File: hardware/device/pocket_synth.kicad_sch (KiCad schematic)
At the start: 7 parts

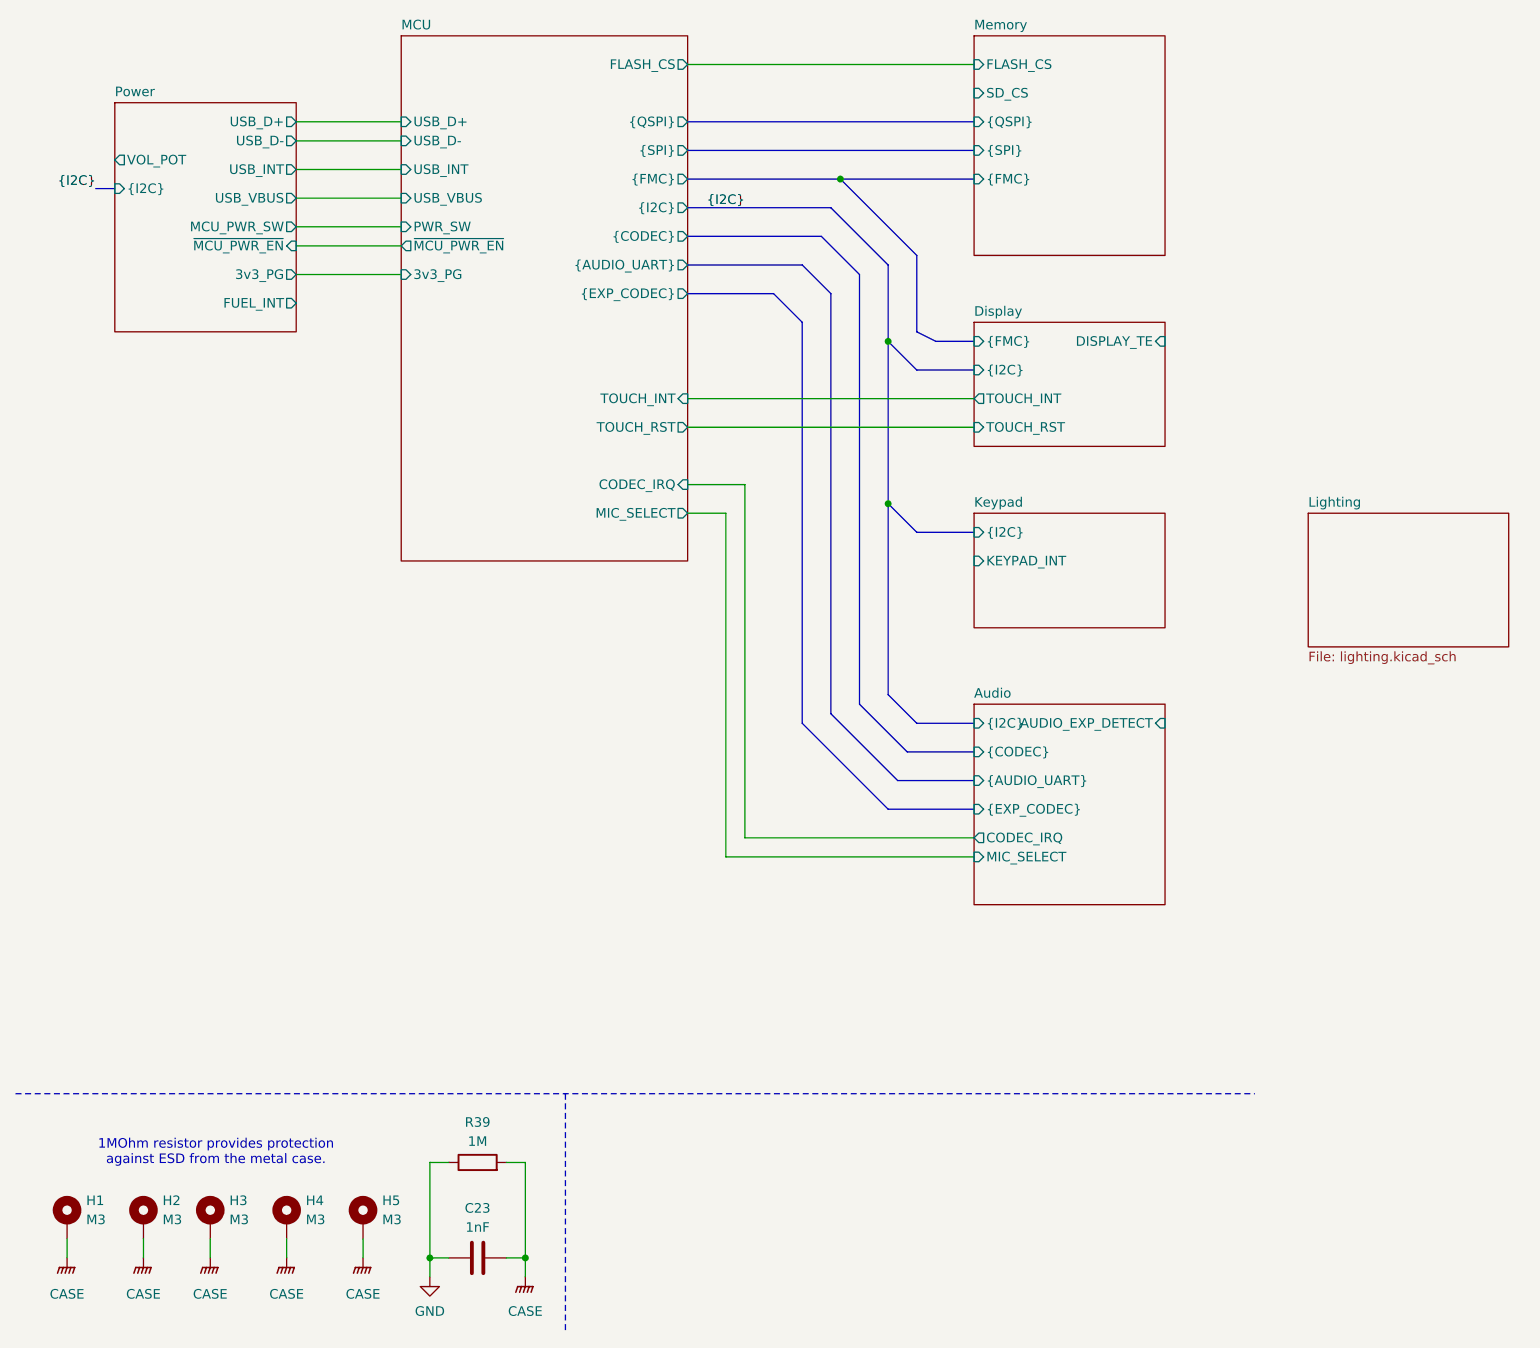
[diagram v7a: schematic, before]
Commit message: feat: start replacing expansion  port with bluetooth module
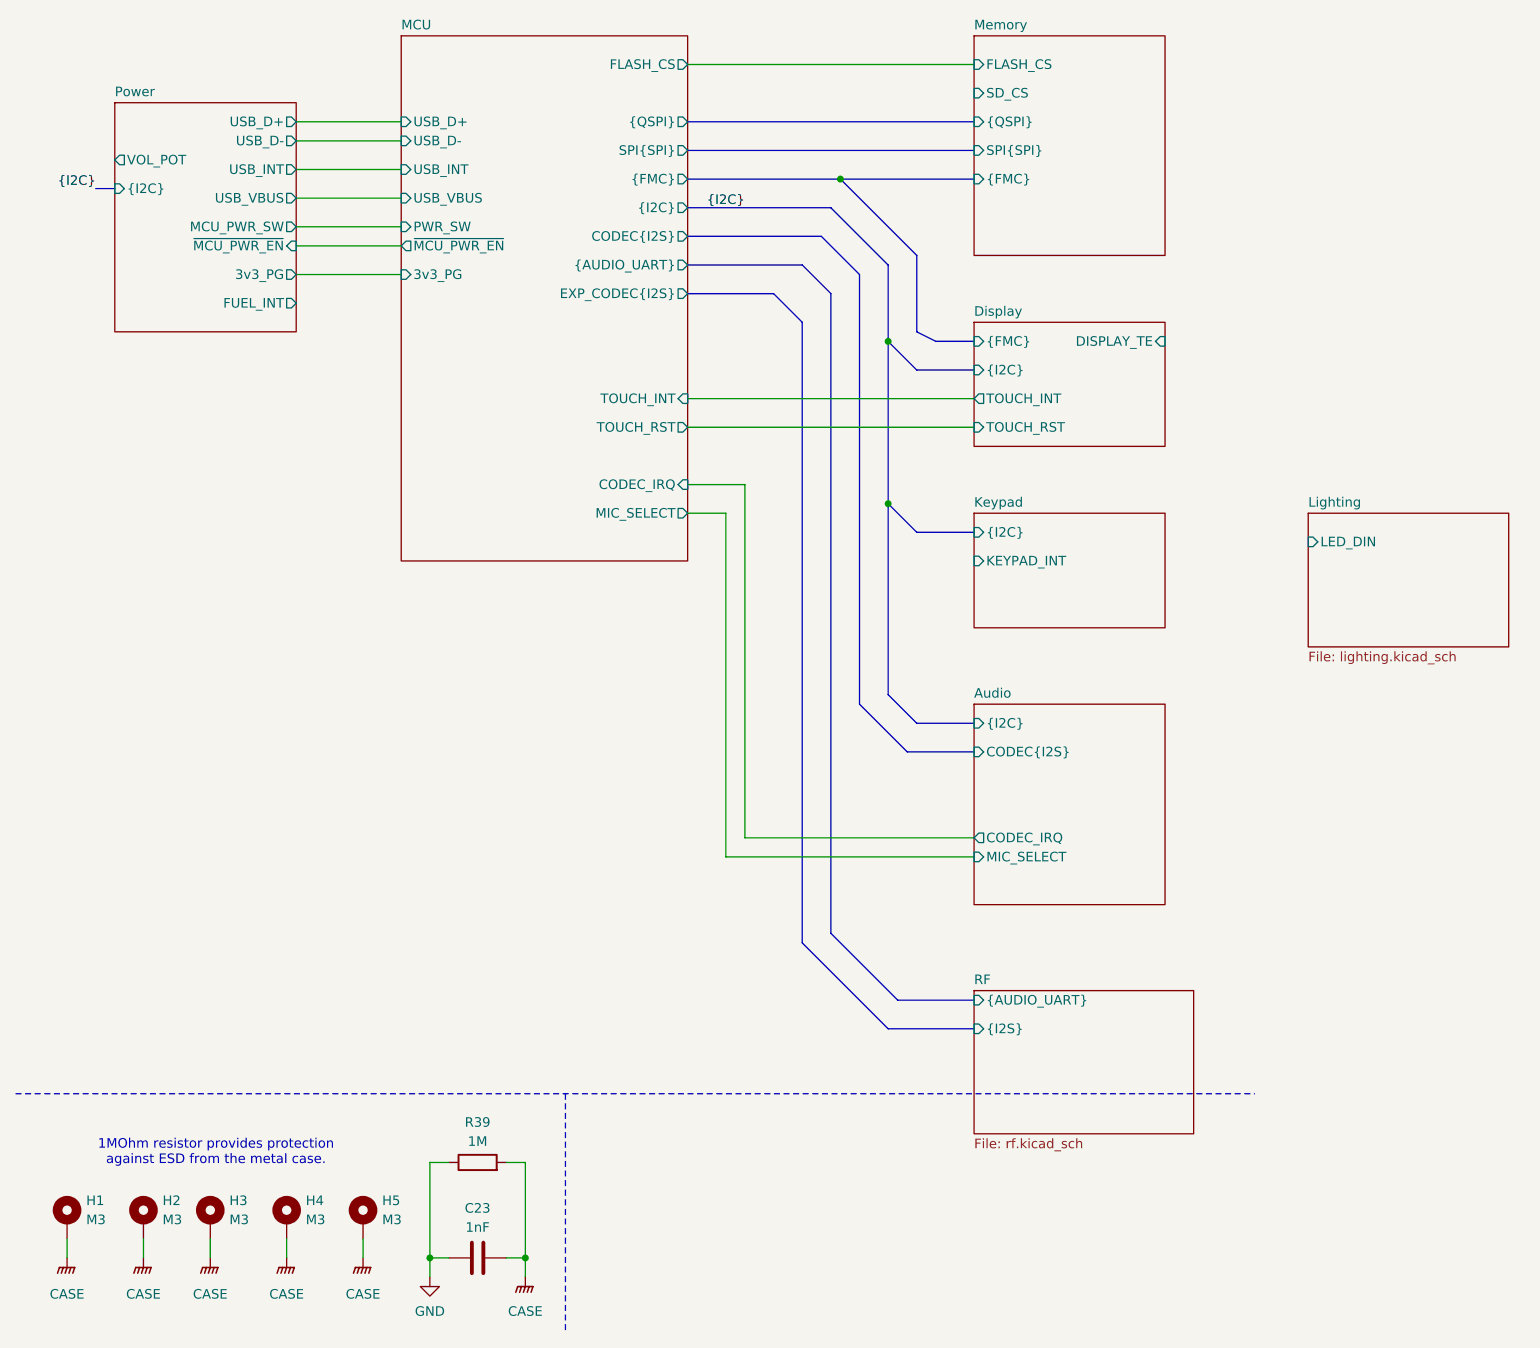
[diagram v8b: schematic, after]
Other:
- added sheet RF (rf.kicad_sch)
- sheet Audio ports: added CODEC{I2S}; removed AUDIO_EXP_DETECT, {AUDIO_UART}, {CODEC}, {EXP_CODEC}
- sheet Lighting ports: added LED_DIN; removed none
- sheet MCU ports: added CODEC{I2S}, EXP_CODEC{I2S}, SPI{SPI}; removed {CODEC}, {EXP_CODEC}, {SPI}
- sheet Memory ports: added SPI{SPI}; removed {SPI}
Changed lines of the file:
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@@
 		)
+	)
+	(bus_alias "I2S"
+		(members "MCLK" "ADCDAT" "DACDAT" "LRCLK" "BCLK")
 	)
 	(text "1MOhm resistor provides protection\nagainst ESD from the metal case."
@@
 		(color 0 0 0 0)
 	)
+	(bus
+		(pts
+			(xy 128.27 157.48) (xy 139.7 157.48)
+		)
+		(stroke
+			(width 0)
+			(type default)
+		)
+	)
 	(wire
 		(pts
@@
 	(bus
 		(pts
+			(xy 116.84 146.05) (xy 128.27 157.48)
+		)
+		(stroke
+			(width 0)
+			(type default)
+		)
+	)
+	(bus
+		(pts
 			(xy 132.08 116.84) (xy 139.7 116.84)
 		)
@@
 	(bus
 		(pts
+			(xy 120.65 144.78) (xy 129.54 153.67)
+		)
+		(stroke
+			(width 0)
+			(type default)
+		)
+	)
+	(bus
+		(pts
 			(xy 101.6 52.07) (xy 119.38 52.07)
 		)
@@
 	(bus
 		(pts
-			(xy 116.84 63.5) (xy 116.84 116.84)
-		)
-		(stroke
-			(width 0)
-			(type default)
-		)
-	)
-	(bus
-		(pts
 			(xy 101.6 40.64) (xy 139.7 40.64)
+		)
+		(stroke
+			(width 0)
+			(type default)
+		)
+	)
+	(bus
+		(pts
+			(xy 130.81 120.65) (xy 139.7 120.65)
+		)
+		(stroke
+			(width 0)
+			(type default)
+		)
+	)
+	(bus
+		(pts
+			(xy 116.84 63.5) (xy 116.84 146.05)
+		)
+		(stroke
+			(width 0)
+			(type default)
+		)
+	)
+	(bus
+		(pts
+			(xy 120.65 59.69) (xy 120.65 144.78)
 		)
 		(stroke
@@
 		)
 	)
-	(bus
-		(pts
-			(xy 120.65 59.69) (xy 120.65 115.57)
-		)
-		(stroke
-			(width 0)
-			(type default)
-		)
-	)
 	(wire
 		(pts
@@
 	(bus
 		(pts
-			(xy 130.81 120.65) (xy 139.7 120.65)
-		)
-		(stroke
-			(width 0)
-			(type default)
-		)
-	)
-	(bus
-		(pts
 			(xy 124.46 114.3) (xy 130.81 120.65)
 		)
@@
 		)
 	)
-	(bus
-		(pts
-			(xy 129.54 124.46) (xy 139.7 124.46)
-		)
-		(stroke
-			(width 0)
-			(type default)
-		)
-	)
 	(wire
 		(pts
@@
 		)
 	)
-	(bus
-		(pts
-			(xy 128.27 128.27) (xy 139.7 128.27)
-		)
-		(stroke
-			(width 0)
-			(type default)
-		)
-	)
 	(wire
 		(pts
@@
 	(bus
 		(pts
-			(xy 120.65 115.57) (xy 129.54 124.46)
-		)
-		(stroke
-			(width 0)
-			(type default)
-		)
-	)
-	(bus
-		(pts
 			(xy 101.6 44.45) (xy 121.92 44.45)
 		)
@@
 	(bus
 		(pts
-			(xy 116.84 116.84) (xy 128.27 128.27)
-		)
-		(stroke
-			(width 0)
-			(type default)
-		)
-	)
-	(bus
-		(pts
 			(xy 119.38 52.07) (xy 124.46 57.15)
+		)
+		(stroke
+			(width 0)
+			(type default)
+		)
+	)
+	(bus
+		(pts
+			(xy 129.54 153.67) (xy 139.7 153.67)
 		)
 		(stroke
@@
 			)
 		)
-		(pin "{SPI}" output
-			(at 101.6 40.64 0)
-			(effects
-				(font
-					(size 1.27 1.27)
-				)
-				(justify right)
-			)
-		)
 		(pin "USB_D+" input
 			(at 63.5 36.83 180)
@@
 			)
 		)
-		(pin "{CODEC}" output
-			(at 101.6 52.07 0)
-			(effects
-				(font
-					(size 1.27 1.27)
-				)
-				(justify right)
-			)
-		)
 		(pin "~{MCU_PWR_EN}" output
 			(at 63.5 53.34 180)
@@
 			)
 		)
-		(pin "{EXP_CODEC}" output
-			(at 101.6 59.69 0)
-			(effects
-				(font
-					(size 1.27 1.27)
-				)
-				(justify right)
-			)
-		)
 		(pin "{QSPI}" output
 			(at 101.6 36.83 0)
@@
 				)
 				(justify left)
+			)
+		)
+		(pin "CODEC{I2S}" output
+			(at 101.6 52.07 0)
+			(effects
+				(font
+					(size 1.27 1.27)
+				)
+				(justify right)
+			)
+		)
+		(pin "EXP_CODEC{I2S}" output
+			(at 101.6 59.69 0)
+			(effects
+				(font
+					(size 1.27 1.27)
+				)
+				(justify right)
+			)
+		)
+		(pin "SPI{SPI}" output
+			(at 101.6 40.64 0)
+			(effects
+				(font
+					(size 1.27 1.27)
+				)
+				(justify right)
 			)
 		)
@@
 	)
 	(sheet
+		(at 139.7 152.4)
+		(size 29.21 19.05)
+		(exclude_from_sim no)
+		(in_bom yes)
+		(on_board yes)
+		(dnp no)
+		(fields_autoplaced yes)
+		(stroke
+			(width 0.1524)
+			(type solid)
+		)
+		(fill
+			(color 0 0 0 0.0000)
+		)
+		(property "Sheetname" "RF"
+			(at 139.7 151.6884 0)
+			(effects
+				(font
+					(size 1.27 1.27)
+				)
+				(justify left bottom)
+			)
+		)
+		(property "Sheetfile" "rf.kicad_sch"
+			(at 139.7 172.0346 0)
+			(effects
+				(font
+					(size 1.27 1.27)
+				)
+				(justify left top)
+			)
+		)
+		(pin "{I2S}" input
+			(at 139.7 157.48 180)
+			(effects
+				(font
+					(size 1.27 1.27)
+				)
+				(justify left)
+			)
+		)
+		(pin "{AUDIO_UART}" input
+			(at 139.7 153.67 180)
+			(effects
+				(font
+					(size 1.27 1.27)
+				)
+				(justify left)
+			)
+		)
+		(instances
+			(project "pocket_synth"
+				(path "/485383b8-00f4-4405-b270-de249939cff4"
+					(page "9")
+				)
+			)
+		)
+	)
+	(sheet
 		(at 139.7 88.9)
 		(size 25.4 15.24)
@@
 			)
 		)
-		(pin "{CODEC}" input
-			(at 139.7 120.65 180)
-			(effects
-				(font
-					(size 1.27 1.27)
-				)
-				(justify left)
-			)
-		)
 		(pin "{I2C}" input
 			(at 139.7 116.84 180)
@@
 			)
 		)
-		(pin "AUDIO_EXP_DETECT" input
-			(at 165.1 116.84 0)
-			(effects
-				(font
-					(size 1.27 1.27)
-				)
-				(justify right)
-			)
-		)
-		(pin "{AUDIO_UART}" input
-			(at 139.7 124.46 180)
-			(effects
-				(font
-					(size 1.27 1.27)
-				)
-				(justify left)
-			)
-		)
 		(pin "MIC_SELECT" input
 			(at 139.7 134.62 180)
@@
 			)
 		)
-		(pin "{EXP_CODEC}" input
-			(at 139.7 128.27 180)
+		(pin "CODEC{I2S}" input
+			(at 139.7 120.65 180)
 			(effects
 				(font
@@
 			)
 		)
-		(pin "{SPI}" input
-			(at 139.7 40.64 180)
-			(effects
-				(font
-					(size 1.27 1.27)
-				)
-				(justify left)
-			)
-		)
 		(pin "{QSPI}" input
 			(at 139.7 36.83 180)
@@
 		(pin "FLASH_CS" input
 			(at 139.7 29.21 180)
+			(effects
+				(font
+					(size 1.27 1.27)
+				)
+				(justify left)
+			)
+		)
+		(pin "SPI{SPI}" input
+			(at 139.7 40.64 180)
 			(effects
 				(font
@@
 			)
 		)
+		(pin "LED_DIN" input
+			(at 184.15 92.71 180)
+			(effects
+				(font
+					(size 1.27 1.27)
+				)
+				(justify left)
+			)
+		)
